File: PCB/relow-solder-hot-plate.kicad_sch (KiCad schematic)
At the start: 52 parts, among them Q1 WSP4409A, Q2 IRLR8726TRPBF, Q3 SS8050

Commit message: simulation and few adjustments
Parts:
- removed C1: 4.7u, Capacitor_SMD:C_0805_2012Metric, symbol Device:C_Small
- removed R?: 10K, Resistor_SMD:R_0603_1608Metric, symbol Device:R_Small
- added C2: 10u, Capacitor_SMD:C_0603_1608Metric, symbol Device:C_Small
- added C?: 68p, Capacitor_SMD:C_0603_1608Metric, symbol Device:C_Small
- R7: renamed from R11; value 10K -> 200K
- gave numbers to parts that had none: 25
- renumbered C2 to C3, C3 to C4, C4 to C5, C5 to C6, R4 to R10, R13 to R11, R5 to R12, R2 to R3
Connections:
- net GND: now also C?.1
- net T_ANALOG: now also C?.2
- net VCC: no longer R3.1
- net at Q1.4 (G), R7.1: now also C2.1
- net at F1.2, Q1.5 (D), Q1.6 (D)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: now also R3.1, C2.2
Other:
- note added: "C2, R7, Q1 limit the inrush current to ~2.6A. The gate voltage on Q1 slowly rises due to C2 charging."
- note added: "R3 discharge the capacitors (15s) otherwise the inrush current limiter won't work and there's a spark risk with the larger caps"
- note removed: "C1, R11, Q1 limit the inrush current to 7.5A. The gate voltage on Q1 slowly rises due to C1 charging. C1 must be discharged on startup for the inrush current limiter to work."
- note removed: "R2 discharge the capacitors when the power plug is disconnected, otherwise the inrush current limiter won't work and there's a spark risk with the larger caps"
- note removed: "TBD"
- moved on the sheet: C1, C3, C4, C5, C6, C7, C8, D1, L1, R2, R3, R4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

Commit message: schematic release
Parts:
- removed J1: USB_C_Receptacle_USB2.0, symbol Connector:USB_C_Receptacle_USB2.0
- removed R10: 4k7, Resistor_SMD:R_0805_2012Metric, symbol Device:R_Small
- added J1: USB_C_Receptacle, Connector_USB:USB_C_Receptacle_HRO_TYPE-C-31-M-12, symbol Connector:USB_C_Receptacle
- added R9: 5K1, Resistor_SMD:R_0603_1608Metric, symbol Device:R_Small
- added TEMP2: LMT85, Package_SO:Texas_R-PDSO-N5, symbol Sensor_Temperature:LM35-LP
- C1, C11, C12, C9: LCSC (none) -> C338036
- C10, C2, C7, C8: LCSC (none) -> C87152
- C3, C4, C5, C6: LCSC (none) -> C88760
- D1, D2: LCSC (none) -> C64885
- F1: LCSC (none) -> C841188
- H1, H2, H3, H4: LCSC (none) -> C551332
- L1: LCSC (none) -> C90319
- Q1: LCSC (none) -> C2880527
- Q2: LCSC (none) -> C81137
- Q3: LCSC (none) -> C444722
- R11: footprint Resistor_SMD:R_0805_2012Metric -> Resistor_SMD:R_0603_1608Metric; LCSC (none) -> C17414
- R12: footprint Resistor_SMD:R_0805_2012Metric -> Resistor_SMD:R_0603_1608Metric; LCSC (none) -> C384295; LCSC Part Number C17513 -> C384295; LCSC Part Number Alternative C95781 -> C384295
- R13, R3: LCSC (none) -> C17414; LCSC Part Number (none) -> C17414; LCSC Part Number Alternative (none) -> C17414
- R14, R15, R16, R8: LCSC Part Number (none) -> C384295; LCSC Part Number Alternative (none) -> C384295
- R7: LCSC (none) -> C5140968
- SW1: footprint Button_Switch_THT:SW_PUSH_6mm -> Button_Switch_THT:SW_PUSH_6mm_H4.3mm; LCSC (none) -> C499289
- TEMP1: LCSC (none) -> C75856
- U1: LCSC (none) -> C444642
- U2: LCSC (none) -> C603176
- U3: LCSC (none) -> C2913206
- gave numbers to parts that had none: 1
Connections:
- net +3V3: now also TEMP2.1 (+VS)
- net CC1: now also J1.A5 (CC1)
- net CC2: now also J1.B5 (CC2)
- net D+: now also J1.A6 (D+), J1.B6 (D+)
- net D-: now also J1.A7 (D-), J1.B7 (D-)
- net GND: now also J1.A1 (GND), J1.A12 (GND), J1.B1 (GND), J1.B12 (GND), J1.S1 (SHIELD), TEMP2.3 (GND)
- net LED_G: now also U3.6 (GPIO2/TOUCH2/ADC1_CH1); no longer U3.7 (GPIO3/TOUCH3/ADC1_CH2)
- net LED_R: now also U3.9 (GPIO5/TOUCH5/ADC1_CH4); no longer U3.6 (GPIO2/TOUCH2/ADC1_CH1)
- net T_ANALOG: now also TEMP2.2 (Vout)
- net VCC: now also R9.1
- net at Q2.1 (G), Q3.3 (C): now also R9.2
- net at F1.1: now also J1.A4 (VBUS), J1.A9 (VBUS), J1.B4 (VBUS), J1.B9 (VBUS)
- no-connect marks 4 -> 41
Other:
- note added: "Alternative package"
- note added: "With a cold heat plate, the current consumption is too high for the power supply, which are both rated at 3A. To reduce the current consumption, a PWM signal MUST be applied to the MOSFET gate during the warmup phase. The PWM frequency must be at least 50 kHz for the filter capacitors to work properly. To calculate the allowed duty cycle, the user must enter the calculated or measured heat trace 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"
- note added: "https://tinyurl.com/7cd25a7f"
- note removed: "A few notes regarding power consumption: With a cold heat plate, the current consumption is probably too high for the DC plug and the power supply, which are both rated at 5A. To reduce the current consumption, a PWM signal MUST be applied to the MOSFET gate during the warmup phase. The PWM frequency must be at least 50 kHz for the filter capacitors to work properly. To calculate the allowed duty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"
- note removed: "https://tinyurl.com/28wkaqm8"
- moved on the sheet: C10, C11, C13, C9, R8, U3

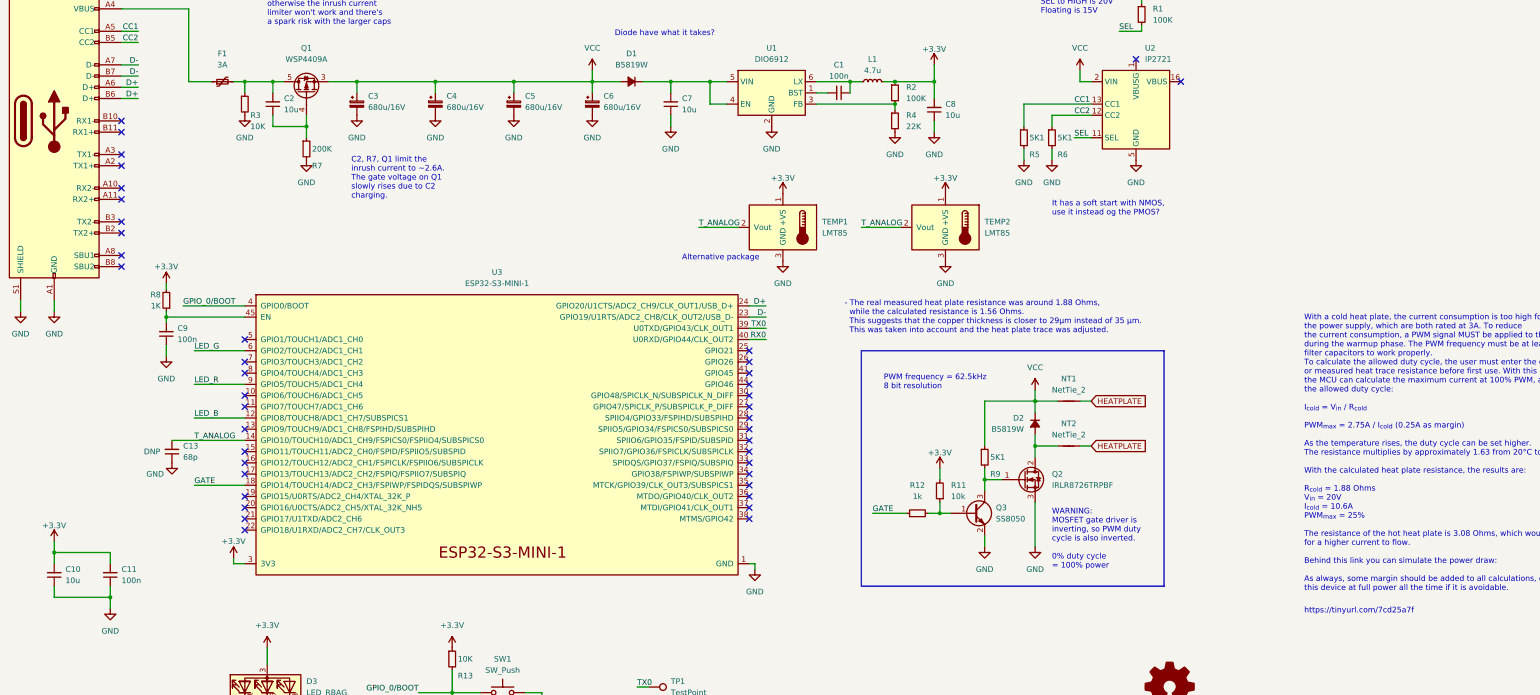
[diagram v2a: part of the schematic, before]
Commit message: Proto (#2)
* FW draft

* web server

* draft gpios

* lmt85

* draft temp control

* dry run

* minor fix

* LEDs are active LOW

* inverted PWM

* captive portal and webserver

* Fix silkscreen and LMT85 footprint

* fix adc attenuation

* fix pwm frequency

* minor fix

* proto

* lmt85 fix

* create mdns task

* green led when connected

* reset leds, when color changes

* 20V@2.25A power supply

* wet run

* fix mdns

* PID
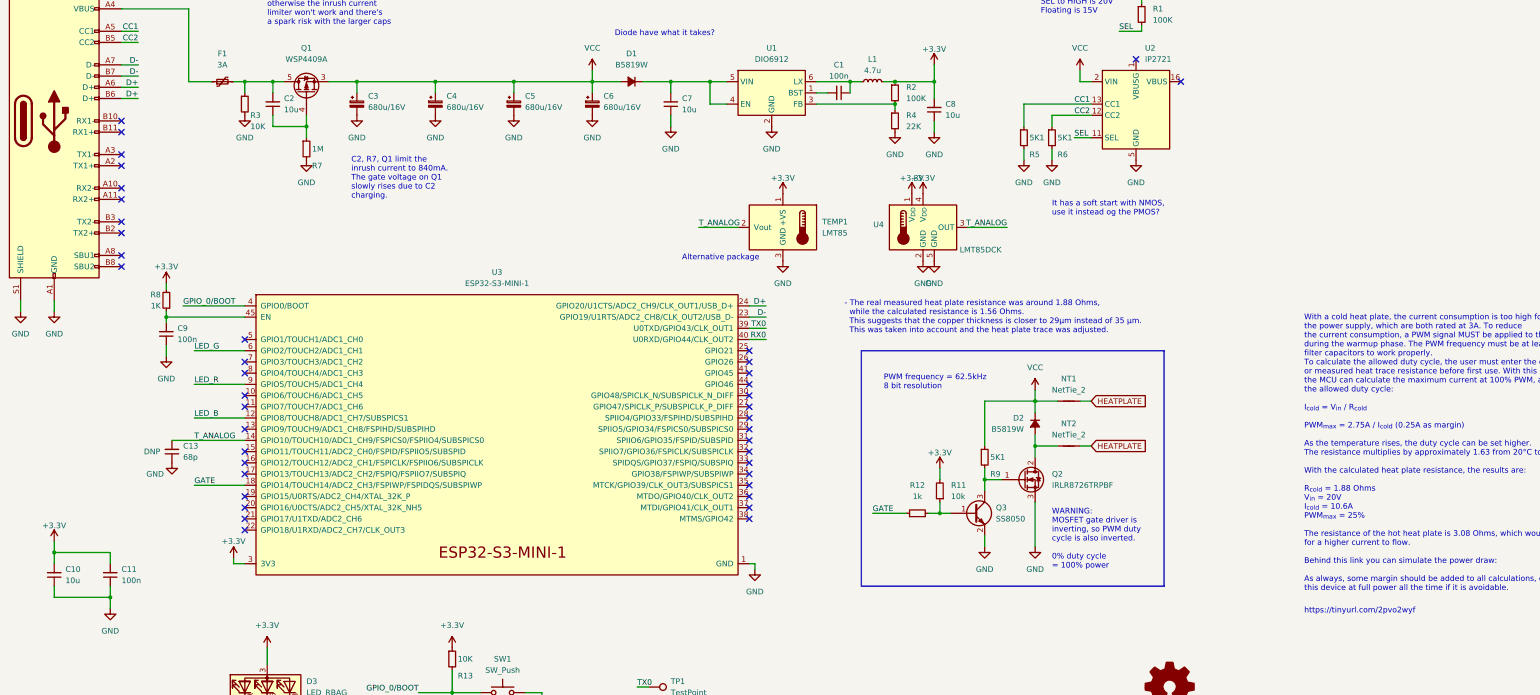
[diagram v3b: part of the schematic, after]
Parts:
- removed TEMP2: LMT85, Package_SO:Texas_R-PDSO-N5, symbol Sensor_Temperature:LM35-LP
- added U4: LMT85DCK, Package_TO_SOT_SMD:SOT-353_SC-70-5, symbol Sensor_Temperature:LMT85DCK
- R7: value 200K -> 1M; LCSC C5140968 -> (none)
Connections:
- net +3V3: now also U4.1 (V_{DD}), U4.4 (V_{DD})
- net GND: now also U4.2 (GND), U4.5 (GND)
- net T_ANALOG: now also U4.3 (OUT)
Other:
- note added: "C2, R7, Q1 limit the inrush current to 840mA. The gate voltage on Q1 slowly rises due to C2 charging."
- note added: "https://tinyurl.com/2pvo2wyf"
- note removed: "C2, R7, Q1 limit the inrush current to ~2.6A. The gate voltage on Q1 slowly rises due to C2 charging."
- note removed: "https://tinyurl.com/7cd25a7f"

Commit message: fix usb-c programmer
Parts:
- removed D1: B5819W, Diode_SMD:D_SOD-123, symbol Device:D_Small_Filled
- R9: value 5K1 -> 100
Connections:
- net +5V: now reaches C7.2, U1.4 (EN), U1.5 (VIN)
- net +5V: now also C2.2, F1.2, Q1.5 (D), Q1.6 (D), Q1.7 (D), Q1.8 (D), R3.1
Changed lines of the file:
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@@
   (junction (at 92.71 36.83) (diameter 0) (color 0 0 0 0)
   )
+  (junction (at 163.83 36.83) (diameter 0) (color 0 0 0 0)
+  )
   (junction (at 73.66 36.83) (diameter 0) (color 0 0 0 0)
   )
@@
   (junction (at 114.3 175.26) (diameter 0) (color 0 0 0 0)
   )
-  (junction (at 163.83 36.83) (diameter 0) (color 0 0 0 0)
-  )
   (junction (at 172.72 36.83) (diameter 0) (color 0 0 0 0)
   )
@@
     (stroke (width 0) (type default))
   )
+  (wire (pts (xy 67.31 33.02) (xy 67.31 36.83))
+    (stroke (width 0) (type default))
+  )
   (wire (pts (xy 67.31 36.83) (xy 73.66 36.83))
     (stroke (width 0) (type default))
@@
     (stroke (width 0) (type default))
   )
+  (wire (pts (xy 163.83 33.02) (xy 163.83 36.83))
+    (stroke (width 0) (type default))
+  )
   (wire (pts (xy 67.31 128.27) (xy 55.88 128.27))
     (stroke (width 0) (type default))
@@
     (stroke (width 0) (type default))
   )
-  (wire (pts (xy 146.05 36.83) (xy 152.4 36.83))
-    (stroke (width 0) (type default))
-  )
   (wire (pts (xy 86.36 36.83) (xy 92.71 36.83))
     (stroke (width 0) (type default))
@@
     (stroke (width 0) (type default))
   )
-  (wire (pts (xy 157.48 36.83) (xy 163.83 36.83))
-    (stroke (width 0) (type default))
-  )
   (wire (pts (xy 73.66 46.99) (xy 81.28 46.99))
     (stroke (width 0) (type default))
@@
     )
   )
+  (symbol (lib_id "power:+5V") (at 67.31 33.02 0) (unit 1)
+    (in_bom yes) (on_board yes) (dnp no) (fields_autoplaced)
+    (property "Reference" "#PWR043" (at 67.31 36.83 0)
+      (effects (font (size 1.27 1.27)) hide)
+    )
+    (property "Value" "+5V" (at 67.31 29.21 0)
+      (effects (font (size 1.27 1.27)))
+    )
+    (property "Footprint" "" (at 67.31 33.02 0)
+      (effects (font (size 1.27 1.27)) hide)
+    )
+    (property "Datasheet" "" (at 67.31 33.02 0)
+      (effects (font (size 1.27 1.27)) hide)
+    )
+    (pin "1")
+    (instances
+      (project "relow-solder-hot-plate"
+        (path "/e63e39d7-6ac0-4ffd-8aa3-1841a4541b55"
+          (reference "#PWR043") (unit 1)
+        )
+      )
+    )
+  )
   (symbol (lib_id "power:GND") (at 214.63 48.26 0) (unit 1)
     (in_bom yes) (on_board yes) (dnp no) (fields_autoplaced)
@@
     )
   )
+  (symbol (lib_id "power:+5V") (at 163.83 33.02 0) (unit 1)
+    (in_bom yes) (on_board yes) (dnp no) (fields_autoplaced)
+    (property "Reference" "#PWR042" (at 163.83 36.83 0)
+      (effects (font (size 1.27 1.27)) hide)
+    )
+    (property "Value" "+5V" (at 163.83 29.21 0)
+      (effects (font (size 1.27 1.27)))
+    )
+    (property "Footprint" "" (at 163.83 33.02 0)
+      (effects (font (size 1.27 1.27)) hide)
+    )
+    (property "Datasheet" "" (at 163.83 33.02 0)
+      (effects (font (size 1.27 1.27)) hide)
+    )
+    (pin "1")
+    (instances
+      (project "relow-solder-hot-plate"
+        (path "/e63e39d7-6ac0-4ffd-8aa3-1841a4541b55"
+          (reference "#PWR042") (unit 1)
+        )
+      )
+    )
+  )
   (symbol (lib_id "Switch:SW_Push") (at 125.73 175.26 0) (unit 1)
     (in_bom yes) (on_board yes) (dnp no) (fields_autoplaced)
@@
       (effects (font (size 1.27 1.27)) (justify left))
     )
-    (property "Value" "5K1" (at 236.22 121.92 0)
+    (property "Value" "100" (at 236.22 121.92 0)
       (effects (font (size 1.27 1.27)) (justify left))
     )
@@
         )
       )
-    )
-  )
-  (symbol (lib_id "Device:D_Small_Filled") (at 154.94 36.83 180) (unit 1)
-    (in_bom yes) (on_board yes) (dnp no) (fields_autoplaced)
-    (property "Reference" "D1" (at 154.94 30.48 0)
-      (effects (font (size 1.27 1.27)))
-    )
-    (property "Value" "B5819W" (at 154.94 33.02 0)
-      (effects (font (size 1.27 1.27)))
-    )
-    (property "Footprint" "Diode_SMD:D_SOD-123" (at 154.94 36.83 90)
-      (effects (font (size 1.27 1.27)) hide)
-    )
-    (property "Datasheet" "~" (at 154.94 36.83 90)
-      (effects (font (size 1.27 1.27)) hide)
-    )
-    (property "LCSC Part Number" "C64885" (at 154.94 36.83 0)
-      (effects (font (size 1.27 1.27)) hide)
-    )
-    (property "LCSC Part Number Alternative" "C109213" (at 154.94 36.83 0)
-      (effects (font (size 1.27 1.27)) hide)
-    )
-    (property "LCSC" "C64885" (at 154.94 36.83 0)
-      (effects (font (size 1.27 1.27)) hide)
-    )
-    (pin "1")
-    (pin "2")
-    (instances
-      (project "relow-solder-hot-plate"
-        (path "/e63e39d7-6ac0-4ffd-8aa3-1841a4541b55"
-          (reference "D1") (unit 1)
-        )
-      )
